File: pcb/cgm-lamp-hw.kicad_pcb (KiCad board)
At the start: 4 copper layers, 80 x 80 mm, 55 parts, among them J1 USB_C_Receptacle_USB2.0_14P, J2 Conn_01x02, J3 DNP, Q1 DMG2305, SW1 RotaryEncoder_Switch_MP, SW2 SW_Push, SW3 SW_Push, SW4 SW_SPST, U1 RT9080-33GJ5, U2 MCP73831-2-OT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

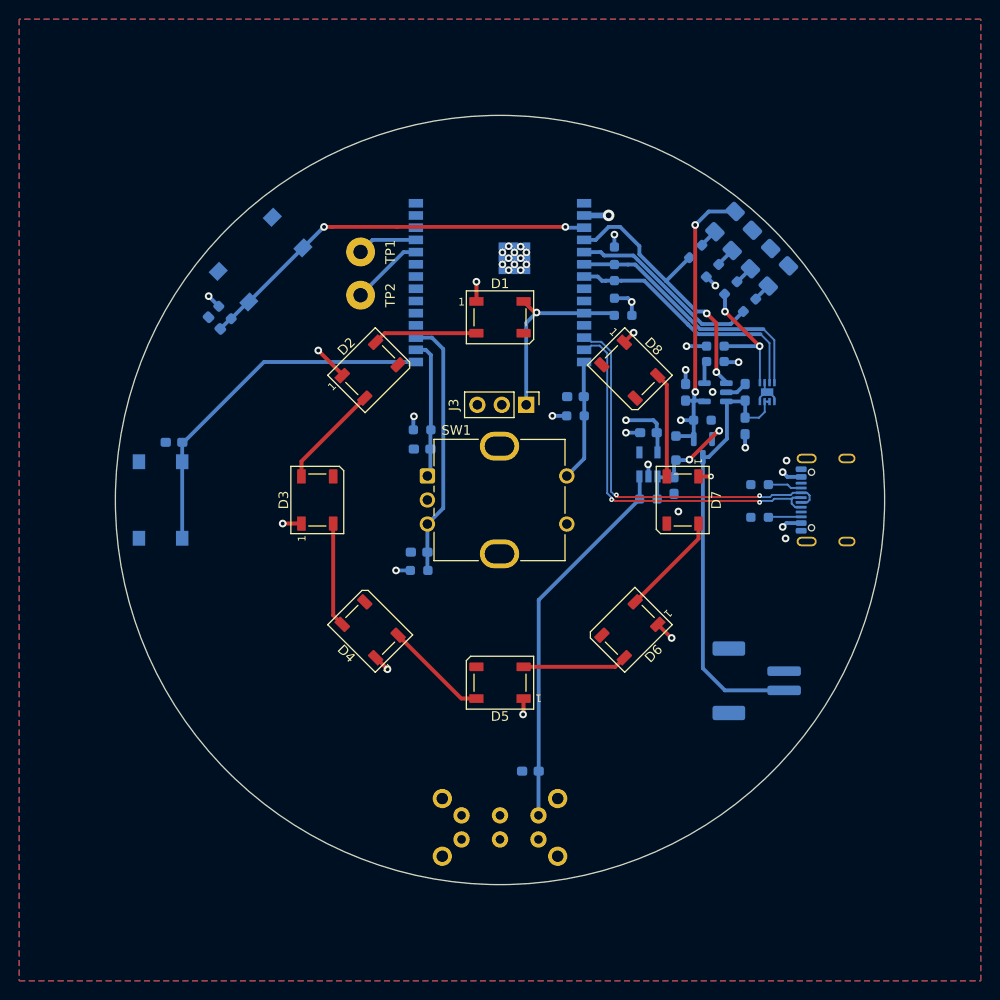
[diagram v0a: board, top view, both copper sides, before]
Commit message: Added ground vias
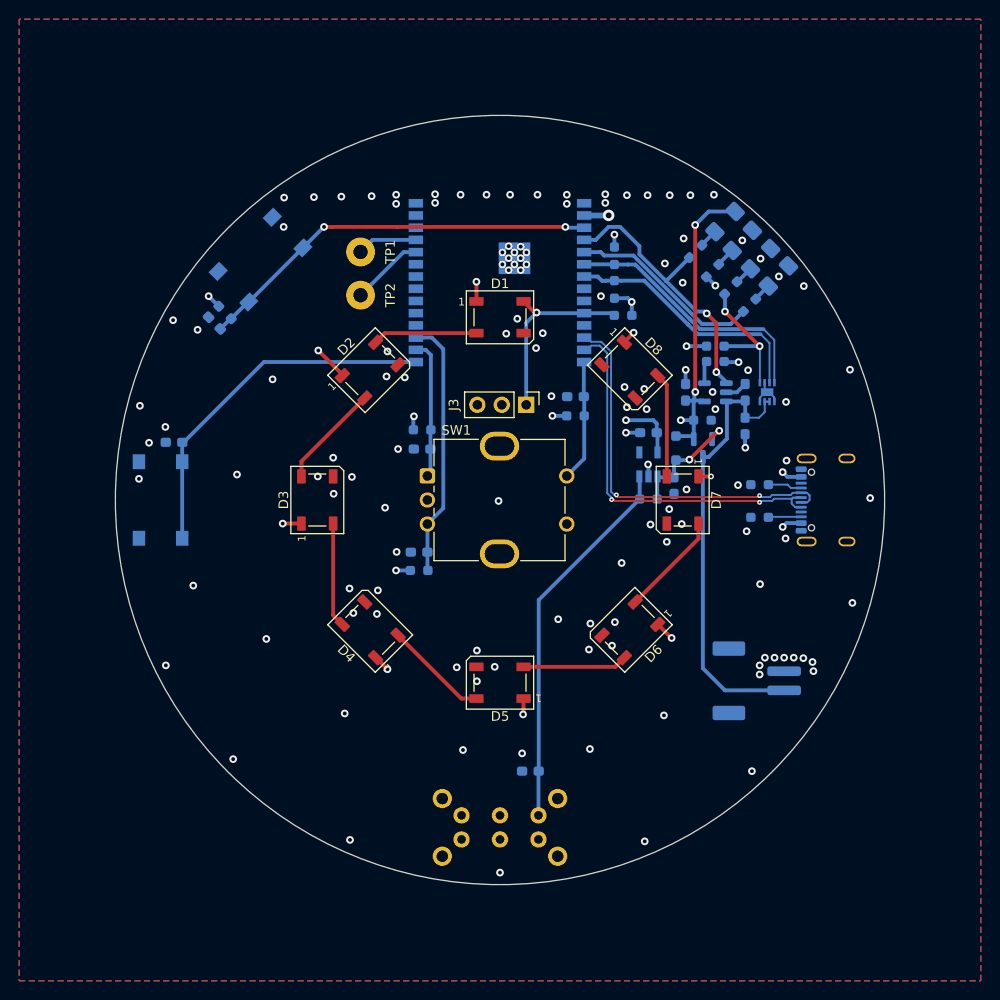
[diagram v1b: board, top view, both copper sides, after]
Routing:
- net GND: vias 21 -> 128

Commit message: Added moutning holes
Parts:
- added H1: MountingHole, MountingHole:MountingHole_3.2mm_M3, F.Cu at (113.5, 120.0)
- added H2: MountingHole, MountingHole:MountingHole_3.2mm_M3, F.Cu at (65.0, 138.0)
- added H3: MountingHole, MountingHole:MountingHole_3.2mm_M3, F.Cu at (46.5, 120.0)
- added H4: MountingHole, MountingHole:MountingHole_3.2mm_M3, F.Cu at (95.0, 138.0)
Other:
- board text added: "240204"
- board text added: "CGM Lamp"
- board text added: "v1"
